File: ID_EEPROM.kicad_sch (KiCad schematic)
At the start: 2 parts, among them U5 M24C64

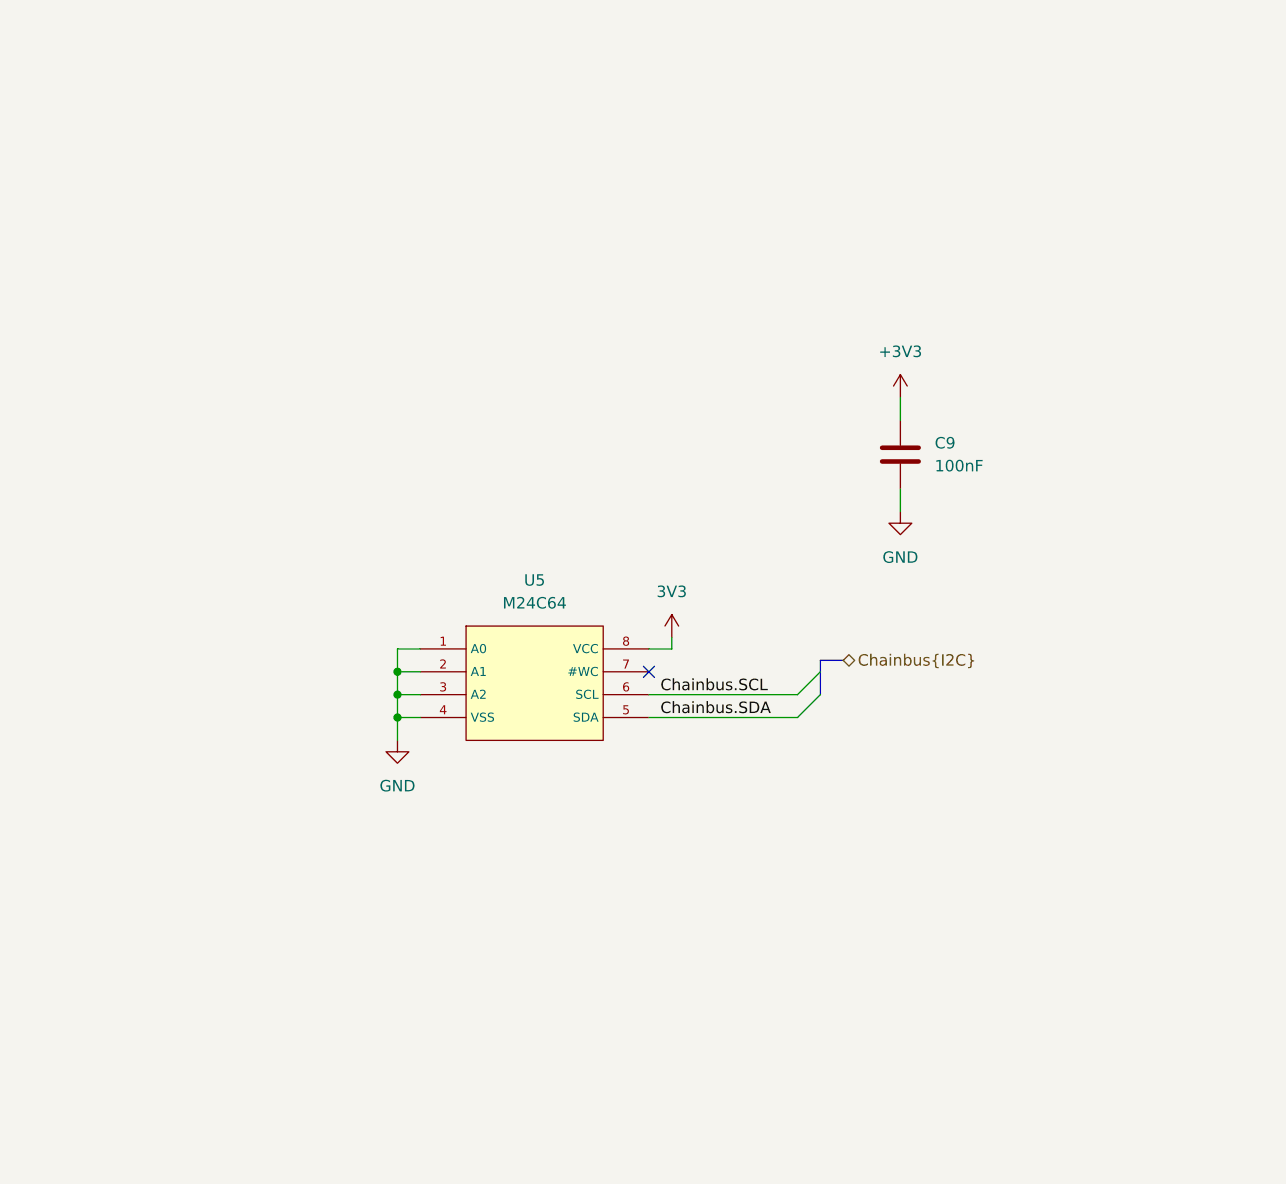
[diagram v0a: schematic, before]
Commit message: finished schematic (without some part numbers)
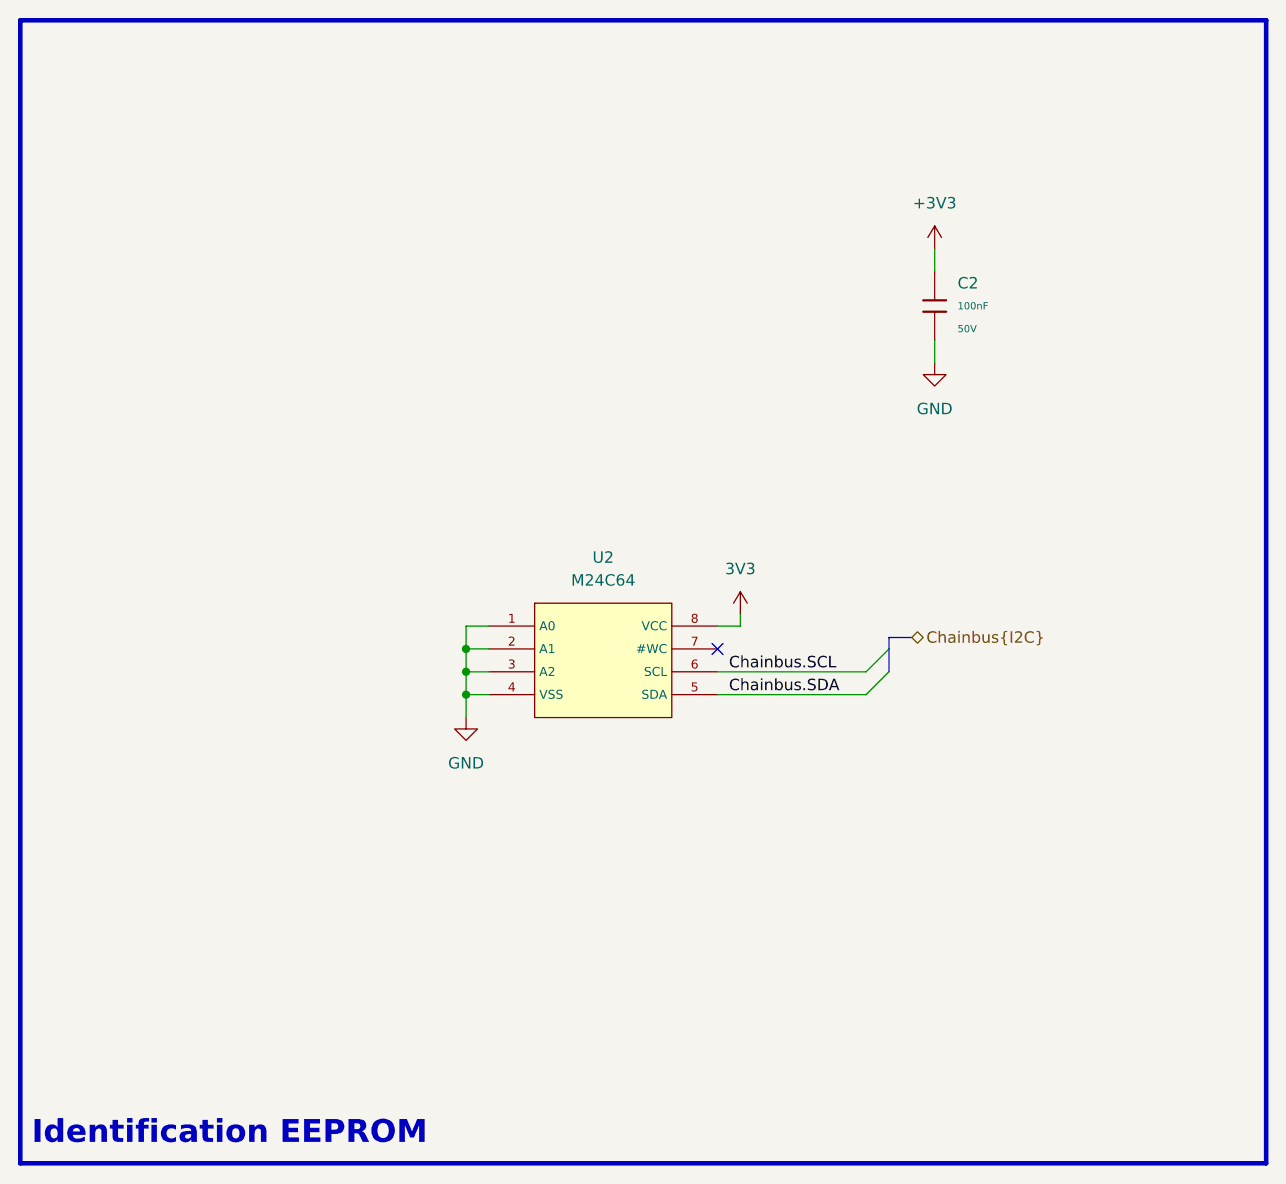
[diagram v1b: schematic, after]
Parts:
- removed C9: 100nF, symbol Device:C
- added C2: 100nF, PCM_JLCPCB:C_0603, symbol PCM_JLCPCB-Capacitors:0603,100nF
- renumbered U5 to U2
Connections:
- net +3V3: now also C2.1
- net GND: now also C2.2
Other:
- note added: "Identification EEPROM"
- moved on the sheet: U2

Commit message: second component placement
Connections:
- net 3V3 is gone; now on net +3V3: U2.8 (VCC)
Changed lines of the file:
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@@
 	(wire
 		(pts
-			(xy 154.94 95.25) (xy 154.94 96.52)
+			(xy 154.94 92.71) (xy 154.94 96.52)
 		)
 		(stroke
@@
 			)
 		)
+		(property "Sim.Device" ""
+			(at 139.7 101.6 0)
+			(effects
+				(font
+					(size 1.27 1.27)
+				)
+				(hide yes)
+			)
+		)
 		(pin "3"
 		)
@@
 		(dnp no)
 		(fields_autoplaced yes)
-		(property "Reference" "#PWR046"
+		(property "Reference" "#PWR045"
 			(at 176.53 73.66 0)
 			(effects
@@
 			(project "MMS2_hat_template_small"
 				(path "/6596548a-44e0-46d8-8624-fd71cf4a3e17/56050d79-5900-47d6-893d-3da0e8bf5810"
-					(reference "#PWR046")
+					(reference "#PWR045")
 					(unit 1)
 				)
@@
 		(dnp no)
 		(fields_autoplaced yes)
-		(property "Reference" "#PWR045"
+		(property "Reference" "#PWR044"
 			(at 176.53 58.42 0)
 			(effects
@@
 		(property "Description" "Power symbol creates a global label with name \"+5V\""
 			(at 176.53 54.61 0)
-			(effects
-				(font
-					(size 1.27 1.27)
-				)
-				(hide yes)
-			)
-		)
-		(pin "1"
-		)
-		(instances
-			(project "MMS2_hat_template_small"
-				(path "/6596548a-44e0-46d8-8624-fd71cf4a3e17/56050d79-5900-47d6-893d-3da0e8bf5810"
-					(reference "#PWR045")
-					(unit 1)
-				)
-			)
-		)
-	)
-	(symbol
-		(lib_id "power:+3.3V")
-		(at 154.94 95.25 0)
-		(unit 1)
-		(exclude_from_sim no)
-		(in_bom yes)
-		(on_board yes)
-		(dnp no)
-		(fields_autoplaced yes)
-		(property "Reference" "#PWR044"
-			(at 154.94 99.06 0)
-			(effects
-				(font
-					(size 1.27 1.27)
-				)
-				(hide yes)
-			)
-		)
-		(property "Value" "3V3"
-			(at 154.94 90.17 0)
-			(effects
-				(font
-					(size 1.27 1.27)
-				)
-			)
-		)
-		(property "Footprint" ""
-			(at 154.94 95.25 0)
-			(effects
-				(font
-					(size 1.27 1.27)
-				)
-				(hide yes)
-			)
-		)
-		(property "Datasheet" ""
-			(at 154.94 95.25 0)
-			(effects
-				(font
-					(size 1.27 1.27)
-				)
-				(hide yes)
-			)
-		)
-		(property "Description" "Power symbol creates a global label with name \"+3.3V\""
-			(at 154.94 95.25 0)
 			(effects
 				(font
@@
 			)
 		)
+		(property "Sim.Device" ""
+			(at 176.53 60.96 0)
+			(effects
+				(font
+					(size 1.27 1.27)
+				)
+				(hide yes)
+			)
+		)
 		(pin "1"
 		)
@@
 				(path "/6596548a-44e0-46d8-8624-fd71cf4a3e17/56050d79-5900-47d6-893d-3da0e8bf5810"
 					(reference "C2")
+					(unit 1)
+				)
+			)
+		)
+	)
+	(symbol
+		(lib_id "power:+5V")
+		(at 154.94 92.71 0)
+		(mirror y)
+		(unit 1)
+		(exclude_from_sim no)
+		(in_bom yes)
+		(on_board yes)
+		(dnp no)
+		(fields_autoplaced yes)
+		(property "Reference" "#PWR043"
+			(at 154.94 96.52 0)
+			(effects
+				(font
+					(size 1.27 1.27)
+				)
+				(hide yes)
+			)
+		)
+		(property "Value" "+3V3"
+			(at 157.48 91.4399 0)
+			(effects
+				(font
+					(size 1.27 1.27)
+				)
+				(justify right)
+			)
+		)
+		(property "Footprint" ""
+			(at 154.94 92.71 0)
+			(effects
+				(font
+					(size 1.27 1.27)
+				)
+				(hide yes)
+			)
+		)
+		(property "Datasheet" ""
+			(at 154.94 92.71 0)
+			(effects
+				(font
+					(size 1.27 1.27)
+				)
+				(hide yes)
+			)
+		)
+		(property "Description" "Power symbol creates a global label with name \"+5V\""
+			(at 154.94 92.71 0)
+			(effects
+				(font
+					(size 1.27 1.27)
+				)
+				(hide yes)
+			)
+		)
+		(pin "1"
+		)
+		(instances
+			(project "MMS3_hat_stepper_controler"
+				(path "/6596548a-44e0-46d8-8624-fd71cf4a3e17/56050d79-5900-47d6-893d-3da0e8bf5810"
+					(reference "#PWR043")
 					(unit 1)
 				)
@@
 		(dnp no)
 		(fields_autoplaced yes)
-		(property "Reference" "#PWR043"
+		(property "Reference" "#PWR042"
 			(at 124.46 113.03 0)
 			(effects
@@
 			(project "MMS2_hat_template_small"
 				(path "/6596548a-44e0-46d8-8624-fd71cf4a3e17/56050d79-5900-47d6-893d-3da0e8bf5810"
-					(reference "#PWR043")
+					(reference "#PWR042")
 					(unit 1)
 				)
